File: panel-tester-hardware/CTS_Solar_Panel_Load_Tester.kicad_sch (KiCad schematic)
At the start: 12 parts, among them J1 Screw_Terminal_01x02, J2 Conn_01x02_Pin, J3 Conn_01x07, J4 Conn_01x03, U1 INA219AxD, U2 YAAJ_BluePill

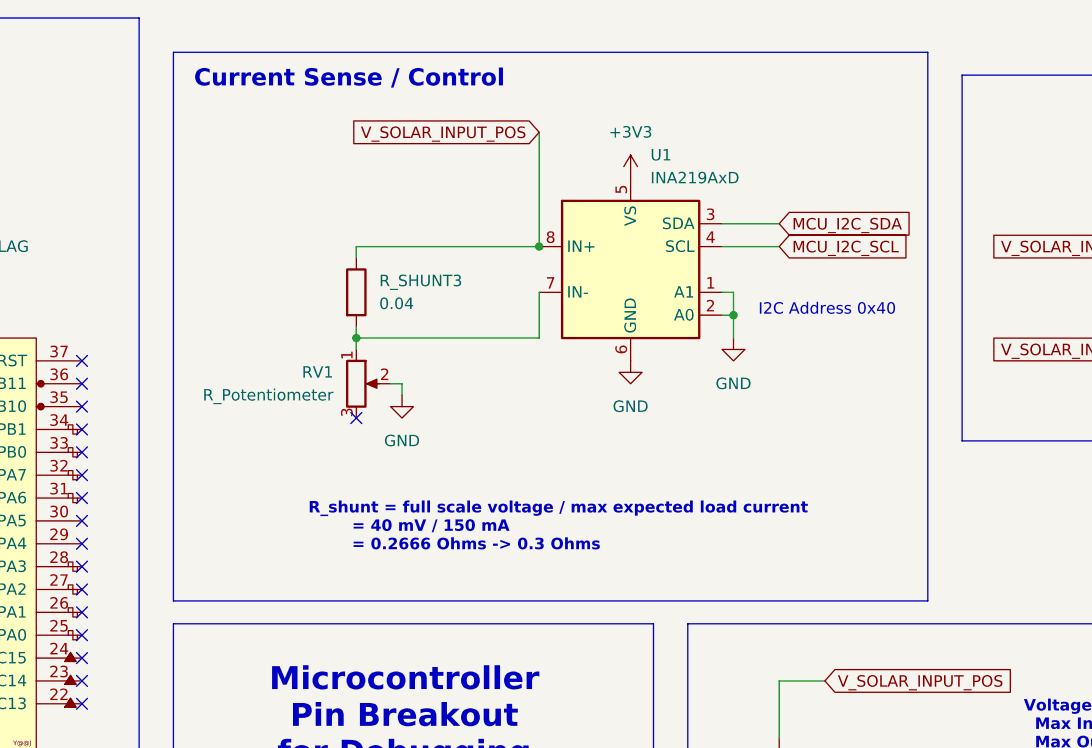
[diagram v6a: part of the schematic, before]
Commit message: Add bypass capacitor
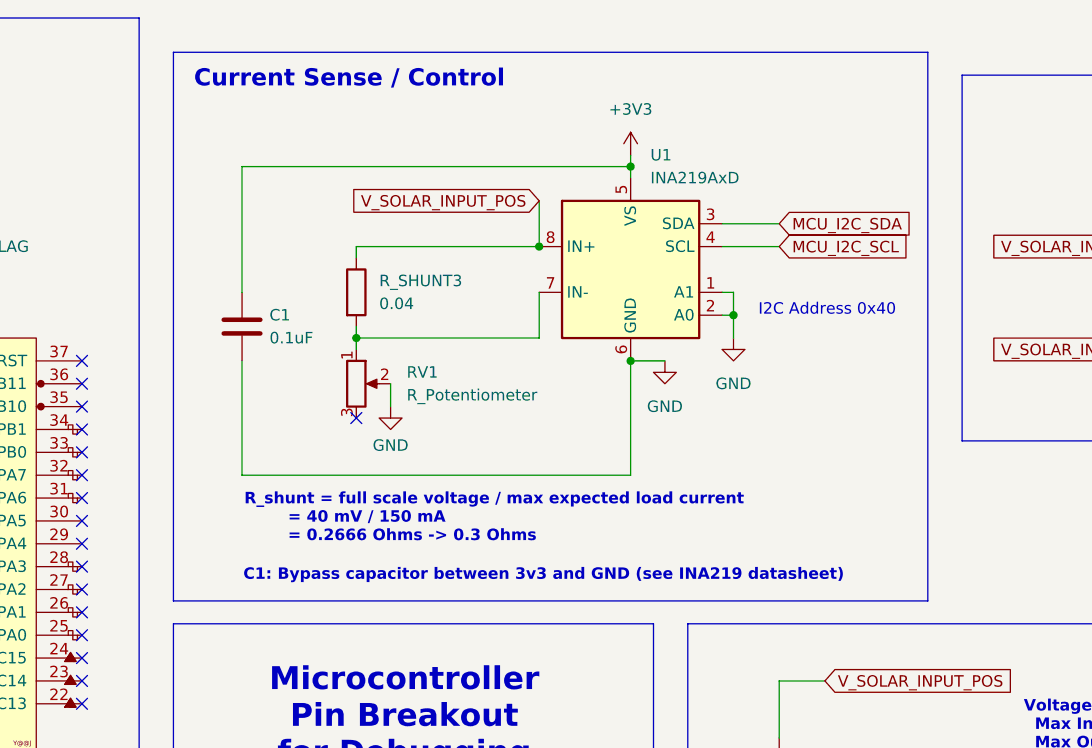
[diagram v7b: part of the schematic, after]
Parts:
- added C1: 0.1uF, Capacitor_SMD:C_1206_3216Metric_Pad1.33x1.80mm_HandSolder, symbol Device:C
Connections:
- net +3V3: now also C1.1
- net GND: now also C1.2
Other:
- note added: "C1: Bypass capacitor between 3v3 and GND (see INA219 datasheet)"
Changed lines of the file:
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@@
 	)
 	(junction
+		(at 157.48 55.88)
+		(diameter 0)
+		(color 0 0 0 0)
+	)
+	(junction
 		(at 127 53.34)
 		(diameter 0)
@@
 		(color 0 0 0 0)
 	)
+	(junction
+		(at 157.48 34.29)
+		(diameter 0)
+		(color 0 0 0 0)
+	)
 	(no_connect
 		(at 55.88 96.52)
@@
 	(wire
 		(pts
+			(xy 157.48 34.29) (xy 114.3 34.29)
+		)
+		(stroke
+			(width 0)
+			(type default)
+		)
+	)
+	(wire
+		(pts
 			(xy 49.53 100.33) (xy 49.53 91.44)
 		)
@@
 	(wire
 		(pts
-			(xy 48.26 71.12) (xy 55.88 71.12)
+			(xy 114.3 34.29) (xy 114.3 48.26)
 		)
 		(stroke
@@
 	(wire
 		(pts
-			(xy 132.08 58.42) (xy 130.81 58.42)
+			(xy 48.26 71.12) (xy 55.88 71.12)
 		)
 		(stroke
@@
 	(wire
 		(pts
+			(xy 161.29 55.88) (xy 157.48 55.88)
+		)
+		(stroke
+			(width 0)
+			(type default)
+		)
+	)
+	(wire
+		(pts
 			(xy 167.64 50.8) (xy 168.91 50.8)
 		)
@@
 	(wire
 		(pts
+			(xy 130.81 58.42) (xy 130.81 60.96)
+		)
+		(stroke
+			(width 0)
+			(type default)
+		)
+	)
+	(wire
+		(pts
 			(xy 133.35 111.76) (xy 137.16 111.76)
 		)
@@
 	(wire
 		(pts
+			(xy 157.48 68.58) (xy 157.48 55.88)
+		)
+		(stroke
+			(width 0)
+			(type default)
+		)
+	)
+	(wire
+		(pts
 			(xy 49.53 91.44) (xy 55.88 91.44)
 		)
@@
 	(wire
 		(pts
+			(xy 157.48 33.02) (xy 157.48 34.29)
+		)
+		(stroke
+			(width 0)
+			(type default)
+		)
+	)
+	(wire
+		(pts
 			(xy 73.66 104.14) (xy 73.66 106.68)
 		)
@@
 	(wire
 		(pts
-			(xy 35.56 83.82) (xy 38.1 83.82)
+			(xy 114.3 68.58) (xy 157.48 68.58)
 		)
 		(stroke
@@
 	(wire
 		(pts
-			(xy 173.99 105.41) (xy 173.99 107.95)
+			(xy 35.56 83.82) (xy 38.1 83.82)
 		)
 		(stroke
@@
 	(wire
 		(pts
-			(xy 133.35 109.22) (xy 137.16 109.22)
+			(xy 173.99 105.41) (xy 173.99 107.95)
 		)
 		(stroke
@@
 	(wire
 		(pts
-			(xy 50.8 58.42) (xy 44.45 58.42)
+			(xy 133.35 109.22) (xy 137.16 109.22)
 		)
 		(stroke
@@
 	(wire
 		(pts
-			(xy 127 43.18) (xy 127 44.45)
+			(xy 50.8 58.42) (xy 44.45 58.42)
 		)
 		(stroke
@@
 	(wire
 		(pts
-			(xy 46.99 96.52) (xy 46.99 88.9)
+			(xy 127 43.18) (xy 127 44.45)
 		)
 		(stroke
@@
 	(wire
 		(pts
-			(xy 35.56 100.33) (xy 49.53 100.33)
+			(xy 46.99 96.52) (xy 46.99 88.9)
 		)
 		(stroke
@@
 	(wire
 		(pts
-			(xy 132.08 58.42) (xy 132.08 59.69)
+			(xy 35.56 100.33) (xy 49.53 100.33)
 		)
 		(stroke
@@
 	(wire
 		(pts
-			(xy 147.32 30.48) (xy 147.32 43.18)
+			(xy 147.32 38.1) (xy 147.32 43.18)
 		)
 		(stroke
@@
 	(wire
 		(pts
+			(xy 157.48 34.29) (xy 157.48 35.56)
+		)
+		(stroke
+			(width 0)
+			(type default)
+		)
+	)
+	(wire
+		(pts
 			(xy 77.47 43.18) (xy 77.47 45.72)
 		)
@@
 		)
 	)
+	(wire
+		(pts
+			(xy 114.3 55.88) (xy 114.3 68.58)
+		)
+		(stroke
+			(width 0)
+			(type default)
+		)
+	)
 	(rectangle
 		(start 15.24 17.78)
@@
 		)
 	)
+	(text "C1: Bypass capacitor between 3v3 and GND (see INA219 datasheet)"
+		(exclude_from_sim no)
+		(at 147.828 79.756 0)
+		(effects
+			(font
+				(size 1.27 1.27)
+				(thickness 0.254)
+				(bold yes)
+			)
+		)
+	)
 	(text "R_shunt = full scale voltage / max expected load current\n		= 40 mV / 150 mA\n		= 0.2666 Ohms -> 0.3 Ohms"
 		(exclude_from_sim no)
-		(at 121.666 74.422 0)
+		(at 114.554 73.406 0)
 		(effects
 			(font
@@
 	(global_label "V_SOLAR_INPUT_POS"
 		(shape input)
-		(at 147.32 30.48 180)
+		(at 147.32 38.1 180)
 		(fields_autoplaced yes)
 		(effects
@@
 		)
 		(property "Intersheetrefs" "${INTERSHEET_REFS}"
-			(at 125.1033 30.48 0)
+			(at 125.1033 38.1 0)
 			(effects
 				(font
@@
 	)
 	(symbol
+		(lib_id "Device:C")
+		(at 114.3 52.07 0)
+		(unit 1)
+		(exclude_from_sim no)
+		(in_bom yes)
+		(on_board yes)
+		(dnp no)
+		(property "Reference" "C1"
+			(at 117.348 50.8 0)
+			(effects
+				(font
+					(size 1.27 1.27)
+				)
+				(justify left)
+			)
+		)
+		(property "Value" "0.1uF"
+			(at 117.348 53.34 0)
+			(effects
+				(font
+					(size 1.27 1.27)
+				)
+				(justify left)
+			)
+		)
+		(property "Footprint" "Capacitor_SMD:C_1206_3216Metric_Pad1.33x1.80mm_HandSolder"
+			(at 115.2652 55.88 0)
+			(effects
+				(font
+					(size 1.27 1.27)
+				)
+				(hide yes)
+			)
+		)
+		(property "Datasheet" "~"
+			(at 114.3 52.07 0)
+			(effects
+				(font
+					(size 1.27 1.27)
+				)
+				(hide yes)
+			)
+		)
+		(property "Description" "Unpolarized capacitor"
+			(at 114.3 52.07 0)
+			(effects
+				(font
+					(size 1.27 1.27)
+				)
+				(hide yes)
+			)
+		)
+		(pin "1"
+		)
+		(pin "2"
+		)
+		(instances
+			(project ""
+				(path "/211b8366-2b1c-422c-86f1-173703c1ab0a"
+					(reference "C1")
+					(unit 1)
+				)
+			)
+		)
+	)
+	(symbol
 		(lib_id "Connector:Screw_Terminal_01x02")
 		(at 236.22 41.91 0)
@@
 		(on_board yes)
 		(dnp no)
-		(fields_autoplaced yes)
 		(property "Reference" "RV1"
-			(at 124.46 57.1499 0)
+			(at 132.588 57.15 0)
 			(effects
 				(font
 					(size 1.27 1.27)
 				)
-				(justify right)
+				(justify left)
 			)
 		)
 		(property "Value" "R_Potentiometer"
-			(at 124.46 59.6899 0)
+			(at 132.588 59.69 0)
 			(effects
 				(font
 					(size 1.27 1.27)
 				)
-				(justify right)
+				(justify left)
 			)
 		)
@@
 	(symbol
 		(lib_id "power:+3.3V")
-		(at 157.48 35.56 0)
+		(at 157.48 33.02 0)
 		(unit 1)
 		(exclude_from_sim no)
@@
 		(fields_autoplaced yes)
 		(property "Reference" "#PWR08"
-			(at 157.48 39.37 0)
+			(at 157.48 36.83 0)
 			(effects
 				(font
@@
 		)
 		(property "Value" "+3V3"
-			(at 157.48 30.48 0)
+			(at 157.48 27.94 0)
 			(effects
 				(font
@@
 		)
 		(property "Footprint" ""
-			(at 157.48 35.56 0)
+			(at 157.48 33.02 0)
 			(effects
 				(font
@@
 		)
 		(property "Datasheet" ""
-			(at 157.48 35.56 0)
+			(at 157.48 33.02 0)
 			(effects
 				(font
@@
 		)
 		(property "Description" "Power symbol creates a global label with name \"+3.3V\""
-			(at 157.48 35.56 0)
+			(at 157.48 33.02 0)
 			(effects
 				(font
@@
 	(symbol
 		(lib_id "power:GND")
-		(at 157.48 55.88 0)
+		(at 161.29 55.88 0)
 		(unit 1)
 		(exclude_from_sim no)
@@
 		(fields_autoplaced yes)
 		(property "Reference" "#PWR02"
-			(at 157.48 62.23 0)
+			(at 161.29 62.23 0)
 			(effects
 				(font
@@
 		)
 		(property "Value" "GND"
-			(at 157.48 60.96 0)
+			(at 161.29 60.96 0)
 			(effects
 				(font
@@
 		)
 		(property "Footprint" ""
-			(at 157.48 55.88 0)
+			(at 161.29 55.88 0)
 			(effects
 				(font
@@
 		)
 		(property "Datasheet" ""
-			(at 157.48 55.88 0)
+			(at 161.29 55.88 0)
 			(effects
 				(font
@@
 		)
 		(property "Description" "Power symbol creates a global label with name \"GND\" , ground"
-			(at 157.48 55.88 0)
+			(at 161.29 55.88 0)
 			(effects
 				(font
@@
 	(symbol
 		(lib_id "power:GND")
-		(at 132.08 59.69 0)
+		(at 130.81 60.96 0)
 		(unit 1)
 		(exclude_from_sim no)
@@
 		(on_board yes)
 		(dnp no)
-		(fields_autoplaced yes)
 		(property "Reference" "#PWR012"
-			(at 132.08 66.04 0)
+			(at 130.81 67.31 0)
 			(effects
 				(font
@@
 		)
 		(property "Value" "GND"
-			(at 132.08 64.77 0)
+			(at 130.81 65.278 0)
 			(effects
 				(font
@@
 		)
 		(property "Footprint" ""
-			(at 132.08 59.69 0)
+			(at 130.81 60.96 0)
 			(effects
 				(font
@@
 		)
 		(property "Datasheet" ""
-			(at 132.08 59.69 0)
+			(at 130.81 60.96 0)
 			(effects
 				(font
@@
 		)
 		(property "Description" "Power symbol creates a global label with name \"GND\" , ground"
-			(at 132.08 59.69 0)
+			(at 130.81 60.96 0)
 			(effects
 				(font

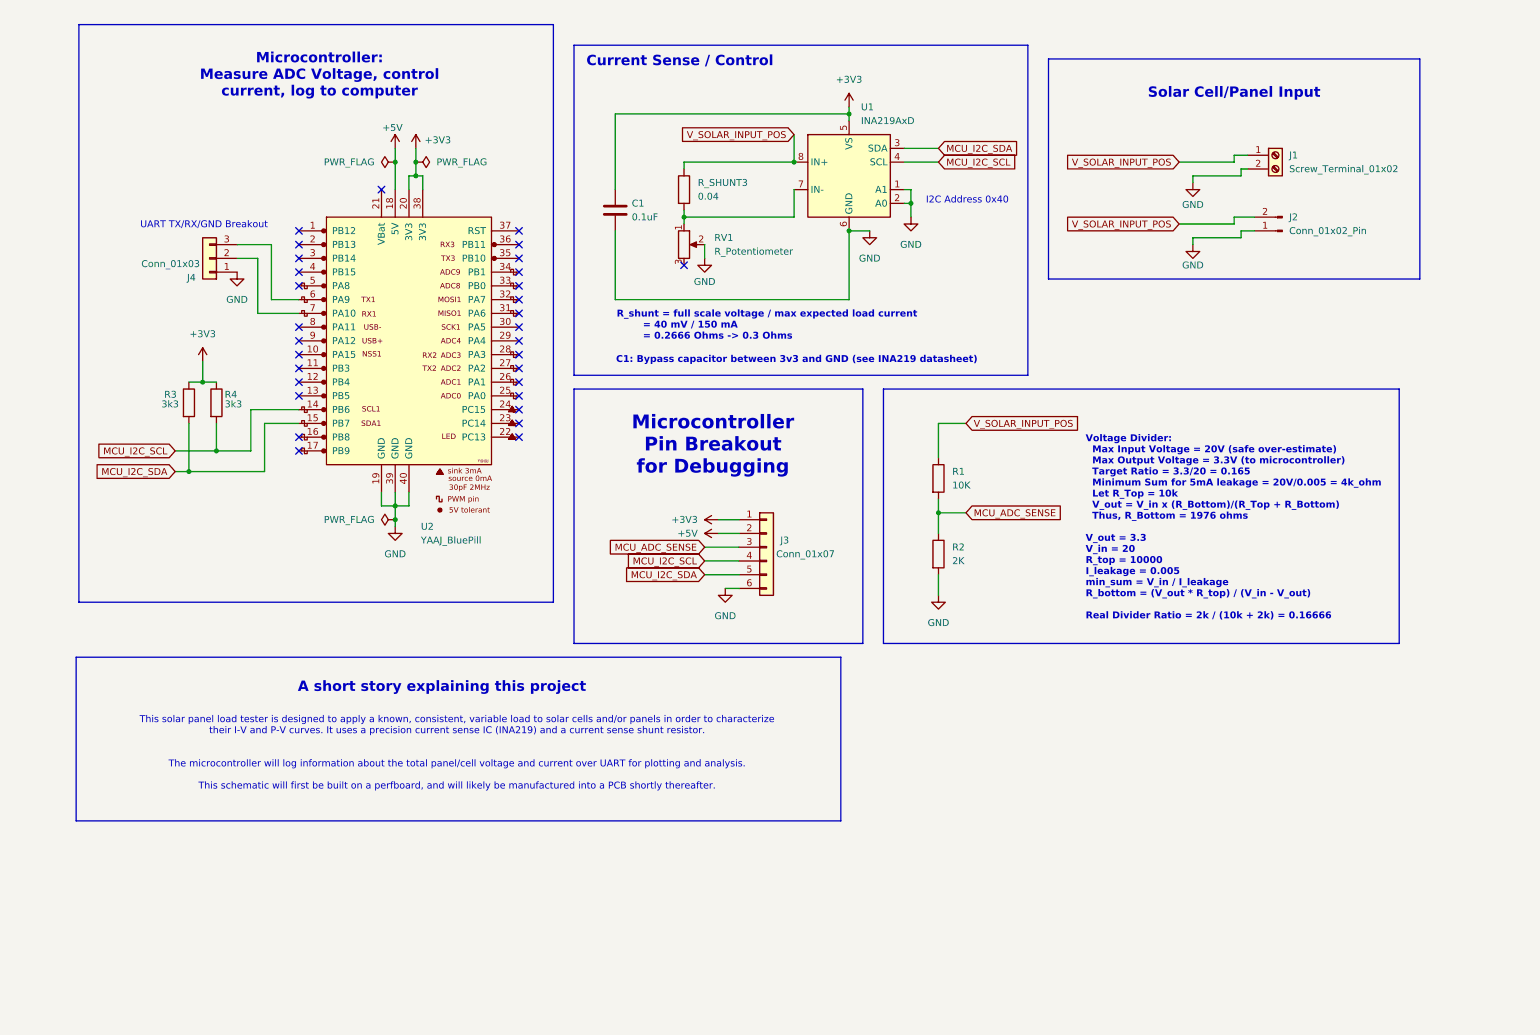
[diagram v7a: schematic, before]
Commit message: made schematic for the amplifier and MOSFET
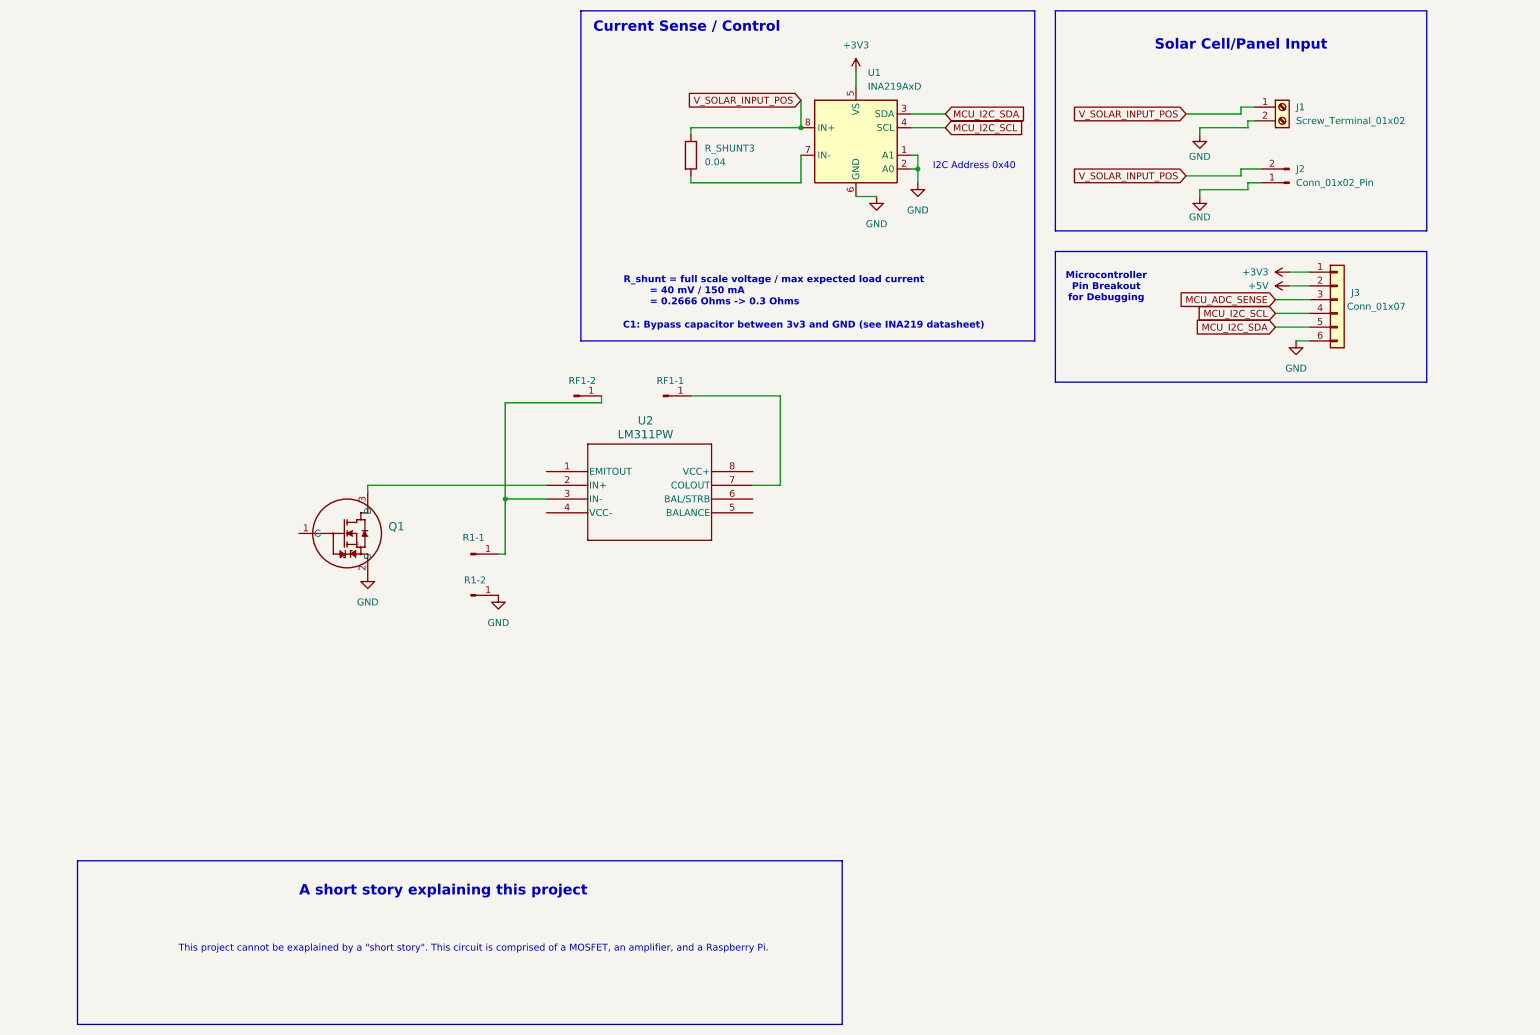
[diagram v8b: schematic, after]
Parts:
- removed C1: 0.1uF, Capacitor_SMD:C_1206_3216Metric_Pad1.33x1.80mm_HandSolder, symbol Device:C
- removed J4: Conn_01x03, Connector_PinHeader_2.54mm:PinHeader_1x03_P2.54mm_Vertical, symbol Connector_Generic:Conn_01x03
- removed R1: 10K, Resistor_SMD:R_1206_3216Metric_Pad1.30x1.75mm_HandSolder, symbol Device:R
- removed R2: 2K, Resistor_SMD:R_1206_3216Metric_Pad1.30x1.75mm_HandSolder, symbol Device:R
- removed R3, R4: 3k3, Resistor_SMD:R_1206_3216Metric_Pad1.30x1.75mm_HandSolder, symbol Device:R
- removed RV1: R_Potentiometer, PotentiometerCustom:3310C101102L, symbol Device:R_Potentiometer
- removed U2: YAAJ_BluePill, BluePill:YAAJ_BluePill_2, symbol YAAJ_BluePill:YAAJ_BluePill
- added Q1: ~, mosfet:TO-236AB_SOT23_NEX, symbol mosfet:2N7002NXAKR
- added R1-1, R1-2, RF1-1, RF1-2: ~, Connector_PinHeader_2.54mm:PinHeader_1x01_P2.54mm_Vertical, symbol Connector:Conn_01x01_Pin
- added U2: LM311PW, PW8, symbol lm311opamp:LM311PW
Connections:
- net GND: now also Q1.2 (S), R1-2.1 (Pin_1)
- new net: R1-1.1 (Pin_1), RF1-2.1 (Pin_1), U2.3 (IN-)
- new net: RF1-1.1 (Pin_1), U2.7 (COLOUT)
- new net: Q1.3 (D), U2.2 (IN+)
- no-connect marks 31 -> 0
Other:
- note added: "This project cannot be exaplained by a {dblquote}short story{dblquote}. This circuit is comprised of a MOSFET, an amplifier, and a Raspberry Pi."
- note removed: "Microcontroller: Measure ADC Voltage, control current, log to computer"
- note removed: "This solar panel load tester is designed to apply a known, consistent, variable load to solar cells and/or panels in order to characterize their I-V and P-V curves. It uses a precision current sense IC (INA219) and a current sense shunt resistor. The microcontroller will log information about the total panel/cell voltage and current over UART for plotting and analysis. This schematic will first b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"
- note removed: "UART TX/RX/GND Breakout"
- note removed: "Voltage Divider: Max Input Voltage = 20V (safe over-estimate) Max Output Voltage = 3.3V (to microcontroller) Target Ratio = 3.3/20 = 0.165 Minimum Sum for 5mA leakage = 20V/0.005 = 4k_ohm Let R_Top = 10k V_out = V_in x (R_Bottom)/(R_Top + R_Bottom) Thus, R_Bottom = 1976 ohms V_out = 3.3 V_in = 20 R_top = 10000 I_leakage = 0.005 min_sum = V_in / I_leakage R_bottom = (V_out * R_top) / (V_in - V_out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"
- moved on the sheet: J1, J2, J3, R_SHUNT3, U1
